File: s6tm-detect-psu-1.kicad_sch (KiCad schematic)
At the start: 60 parts, among them J1 USB_C_Receptacle_USB2.0_14P, J6 Conn_01x02, J7 Conn_01x02, U1 TPS62933, U3 TPS259470x, U5 TPS259470x, U7 TPS259470x, U8 TPS259470x

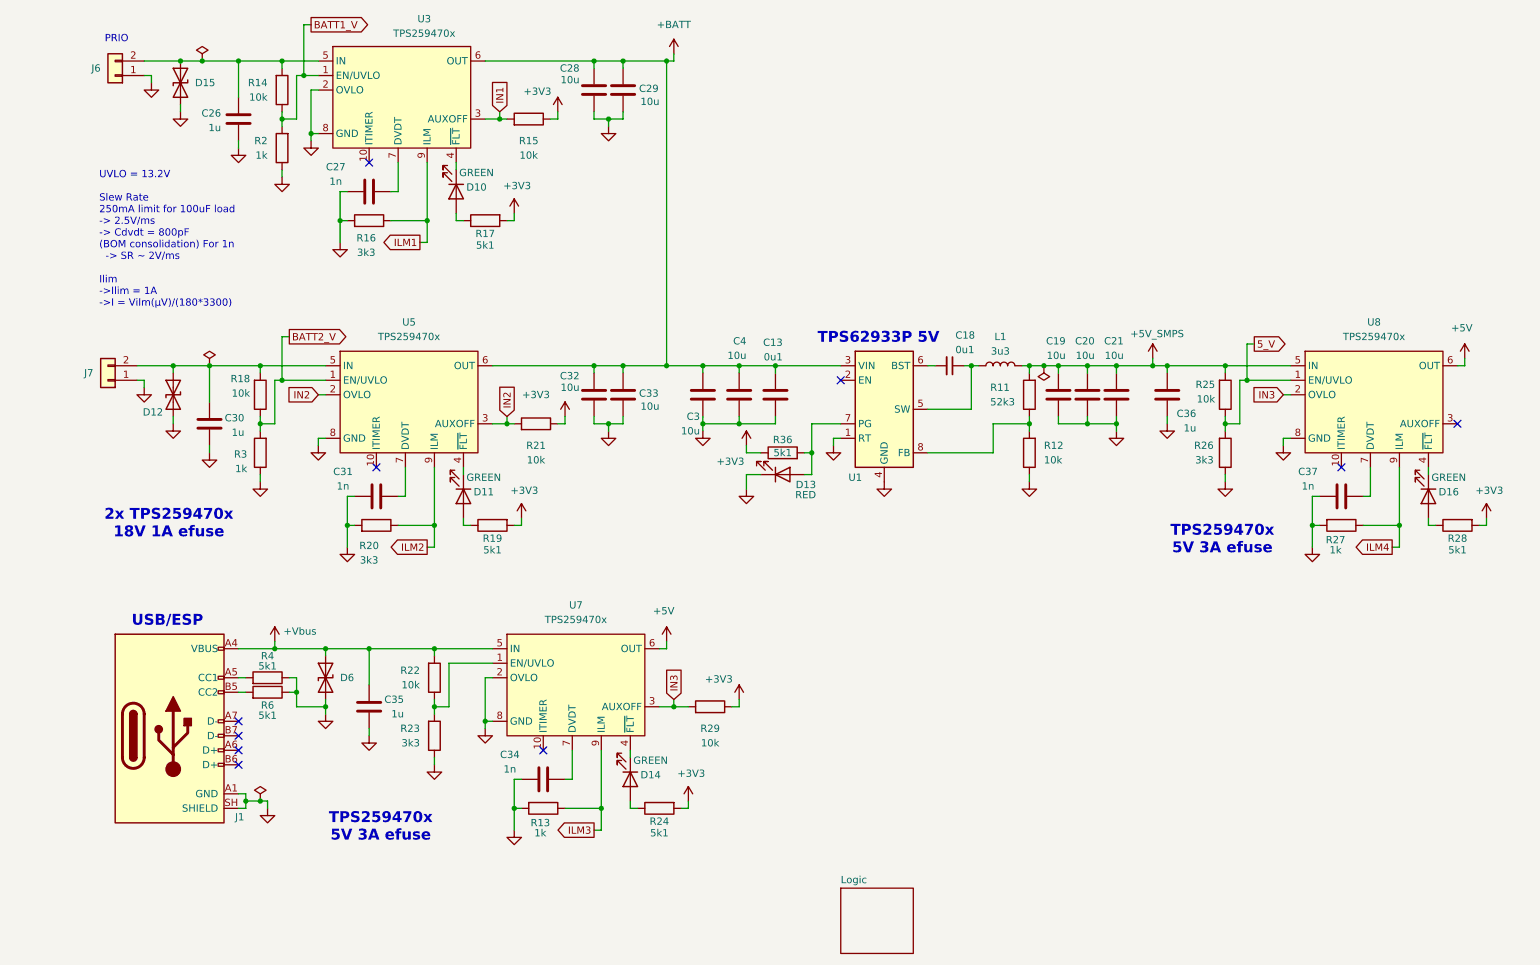
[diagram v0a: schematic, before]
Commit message: schem: add +5v bulk output caps
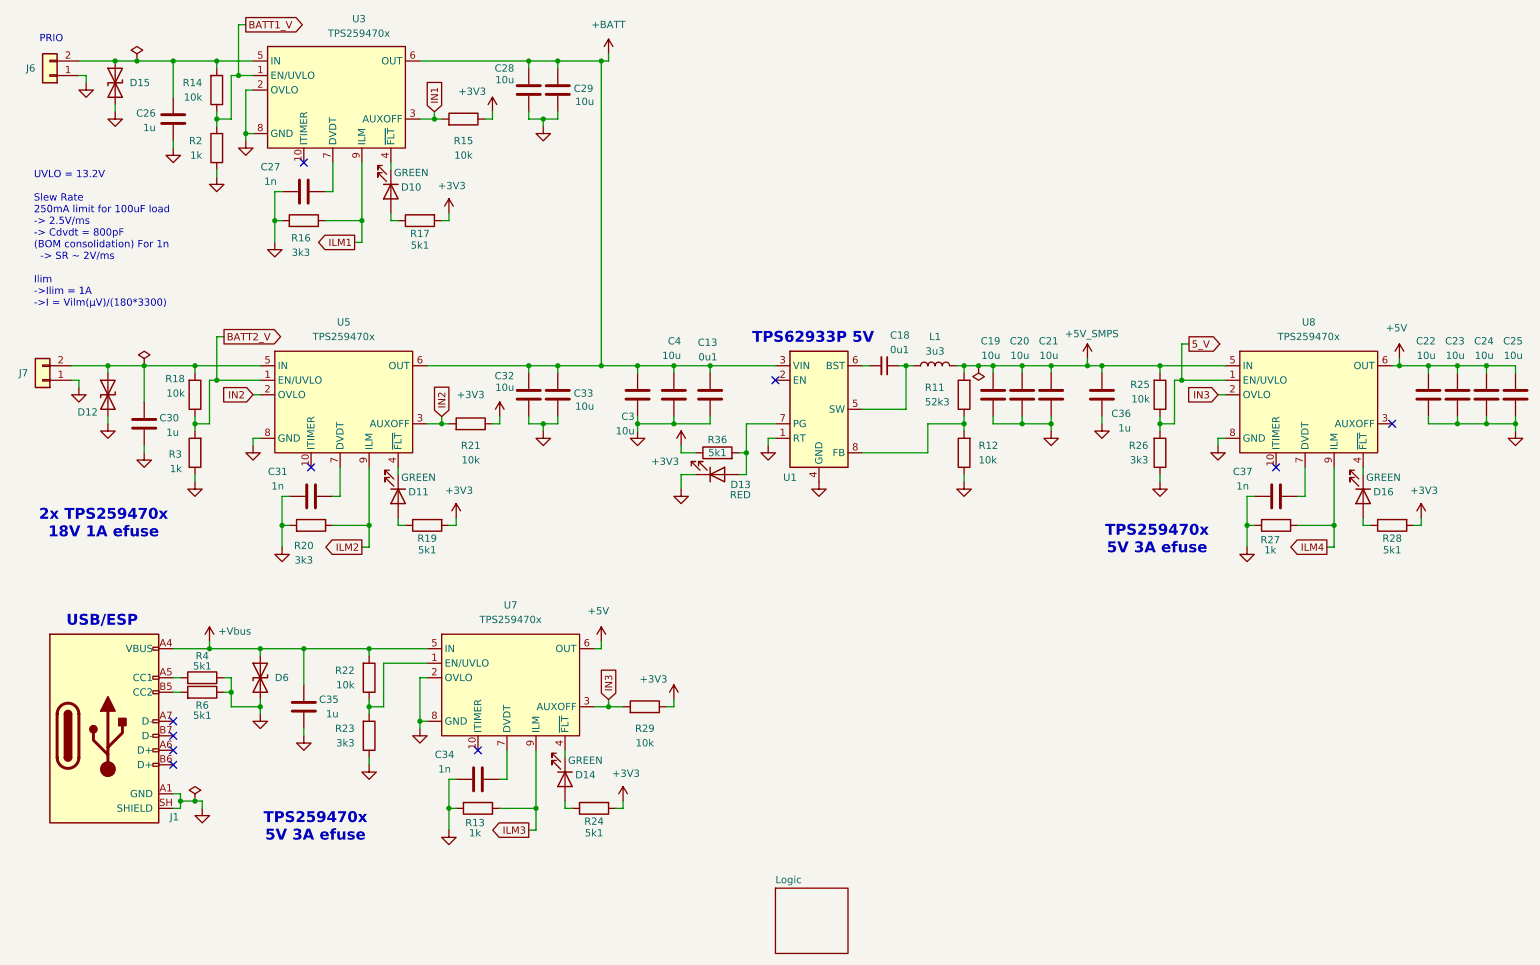
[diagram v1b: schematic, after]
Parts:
- added C22, C23, C24, C25: 10u, Capacitor_SMD:C_0805_2012Metric, symbol Device:C
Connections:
- net +5V: now also C22.1, C23.1, C24.1, C25.1
- net GND: now also C22.2, C23.2, C24.2, C25.2
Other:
- moved on the sheet: C13, C18, C19, C20, C21, C26, C27, C28, C29, C3, C30, C31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

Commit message: schem: connect efuses to mcu
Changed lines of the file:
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@@
 	)
 	(global_label "IN1"
-		(shape input)
+		(shape output)
 		(at 88.9 44.45 90)
 		(fields_autoplaced yes)
@@
 	)
 	(global_label "IN2"
-		(shape input)
+		(shape output)
 		(at 90.17 97.79 90)
 		(fields_autoplaced yes)
@@
 	)
 	(global_label "IN3"
-		(shape input)
+		(shape output)
 		(at 119.38 147.32 90)
 		(fields_autoplaced yes)

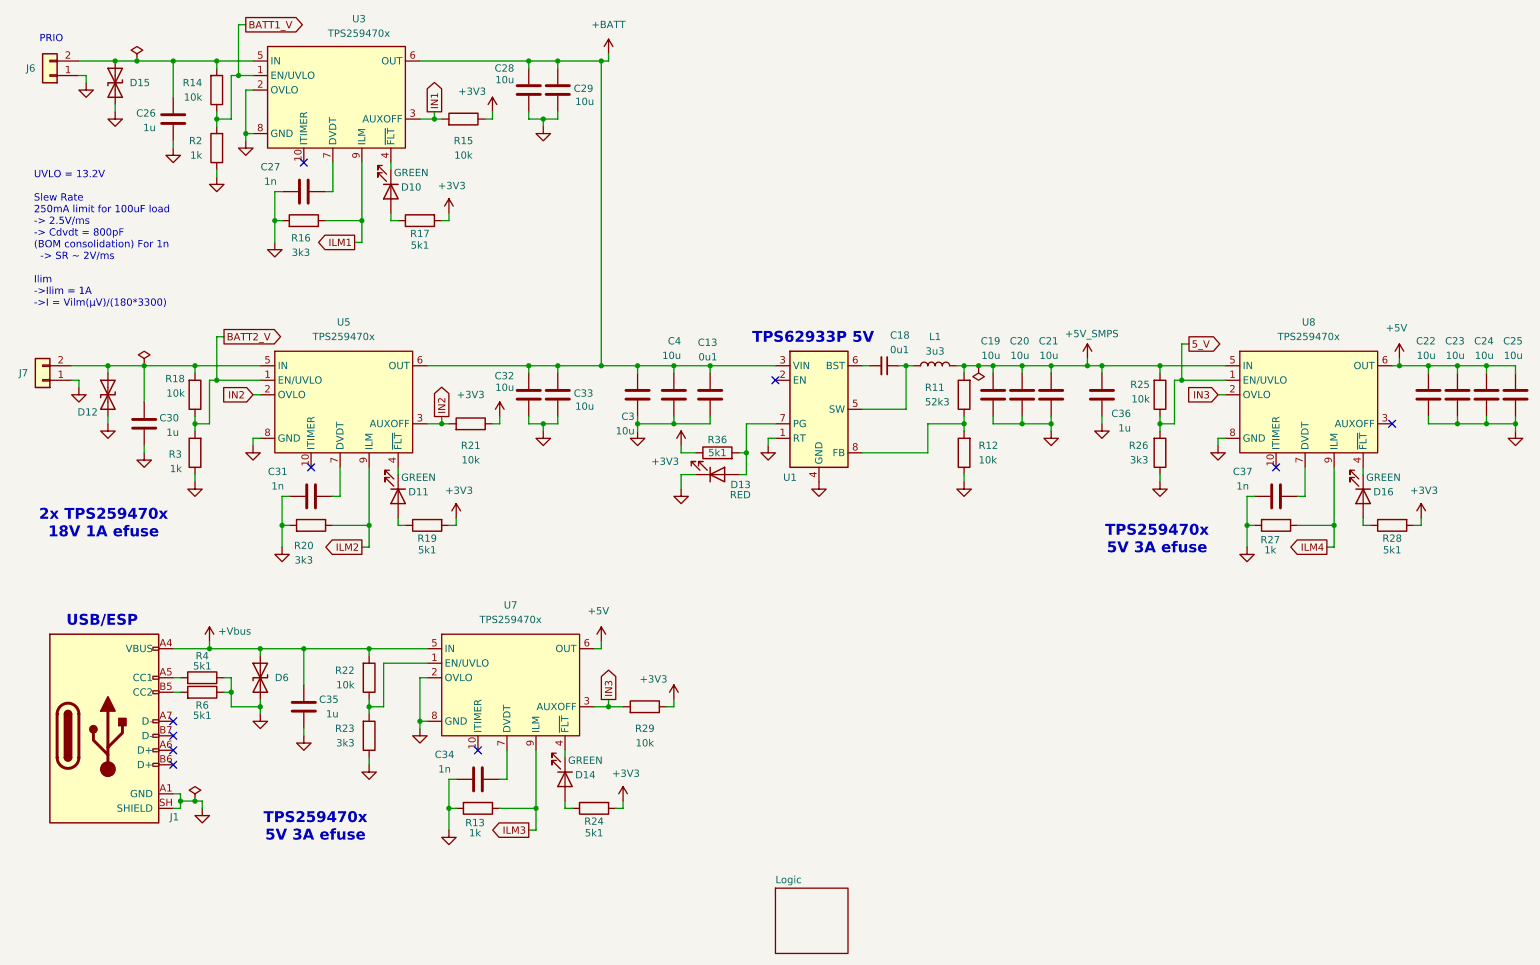
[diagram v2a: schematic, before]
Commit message: schem: add test points
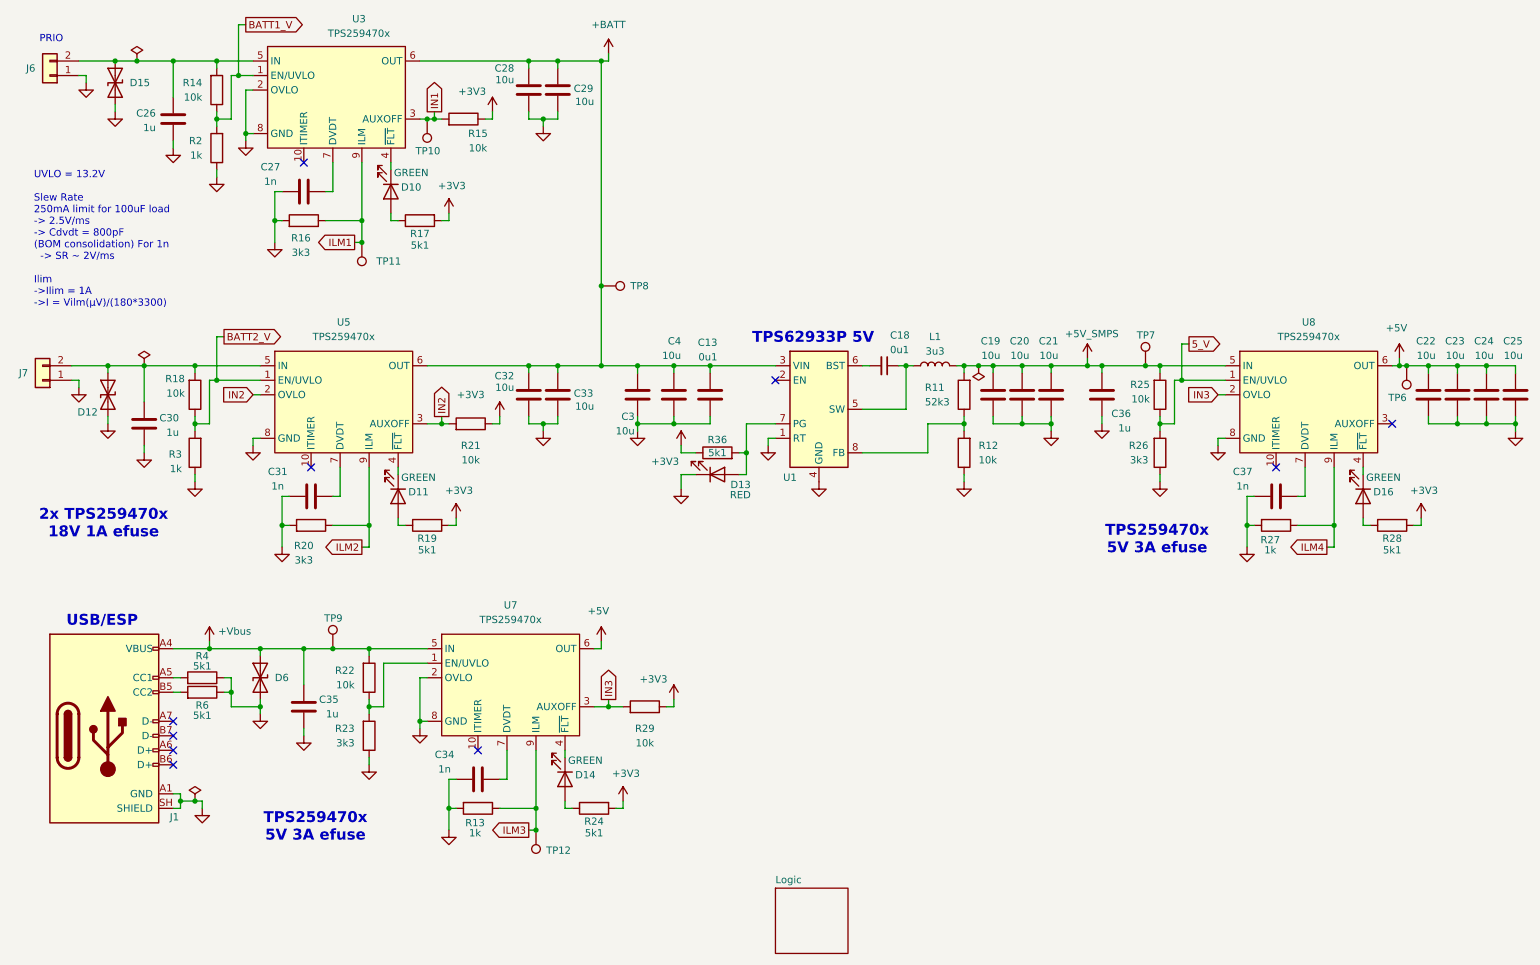
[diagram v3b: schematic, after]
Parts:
- added TP10, TP11, TP12, TP6, TP7, TP8, TP9: TestPoint, TestPoint:TestPoint_Pad_D2.0mm, symbol Connector:TestPoint
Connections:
- net +5V: now also TP6.1
- net +5V_SMPS: now also TP7.1
- net +BATT: now also TP8.1
- net +Vbus: now also TP9.1
- net ILM1: now also TP11.1
- net ILM3: now also TP12.1
- net IN1: now also TP10.1

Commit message: schem: add current measure jumpers
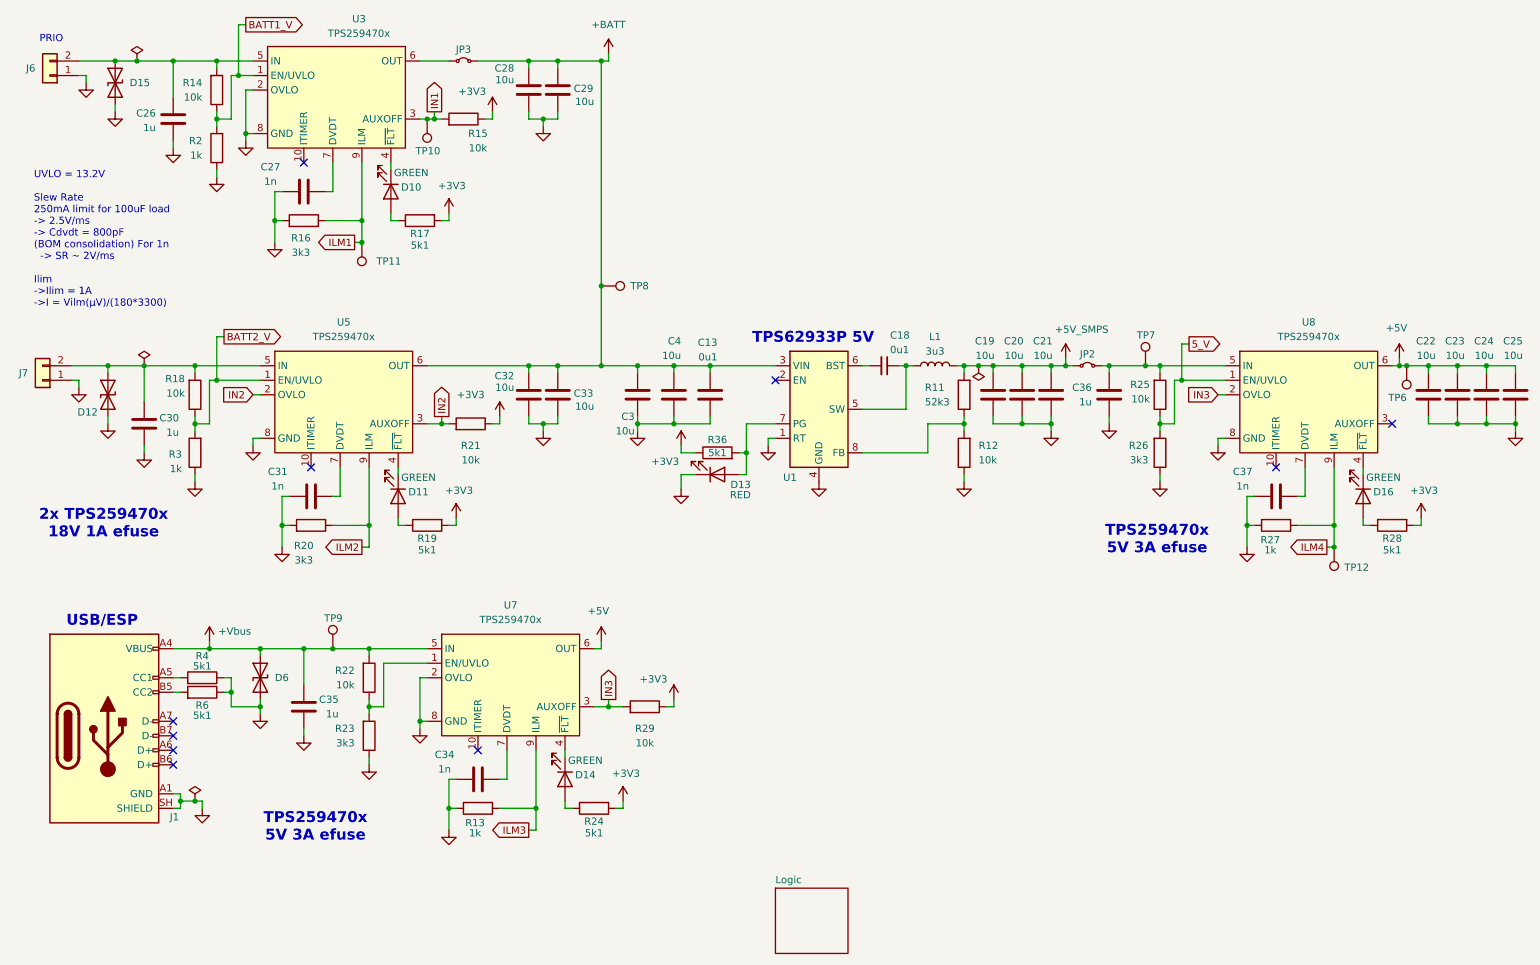
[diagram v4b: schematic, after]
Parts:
- added JP2, JP3: Jumper_2_Small_Bridged, Connector_PinHeader_2.54mm:PinHeader_1x02_P2.54mm_Vertical, symbol Jumper:Jumper_2_Small_Bridged
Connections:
- net +5V_SMPS: now also JP2.1 (A); no longer C36.2, R25.2, TP7.1, U8.5 (IN)
- net +BATT: now also JP3.2 (B); no longer U3.6 (OUT)
- net ILM3: no longer TP12.1
- net ILM4: now also TP12.1
- new net: C36.2, JP2.2 (B), R25.2, TP7.1, U8.5 (IN)
- new net: JP3.1 (A), U3.6 (OUT)
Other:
- moved on the sheet: C36

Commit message: schem: add missing parts to BOM
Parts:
- JP2, JP3: now left out of the parts list
- U3, U5, U7, U8: Basic (none) -> X; JLCPCB Part # (none) -> C3662799; Manufacturer (none) -> Texas Instruments; Manufacturer Part Number (none) -> TPS259470ARPWR
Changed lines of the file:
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@@
 			)
 		)
+		(property "Basic" "X"
+			(at 102.87 143.51 0)
+			(hide yes)
+			(show_name no)
+			(do_not_autoplace no)
+			(effects
+				(font
+					(size 1.27 1.27)
+				)
+			)
+		)
+		(property "JLCPCB Part #" "C3662799"
+			(at 102.87 143.51 0)
+			(hide yes)
+			(show_name no)
+			(do_not_autoplace no)
+			(effects
+				(font
+					(size 1.27 1.27)
+				)
+			)
+		)
+		(property "Manufacturer" "Texas Instruments"
+			(at 102.87 143.51 0)
+			(hide yes)
+			(show_name no)
+			(do_not_autoplace no)
+			(effects
+				(font
+					(size 1.27 1.27)
+				)
+			)
+		)
+		(property "Manufacturer Part Number" "TPS259470ARPWR"
+			(at 102.87 143.51 0)
+			(hide yes)
+			(show_name no)
+			(do_not_autoplace no)
+			(effects
+				(font
+					(size 1.27 1.27)
+				)
+			)
+		)
 		(pin "1"
 		)
@@
 			)
 		)
+		(property "Basic" "X"
+			(at 73.66 93.98 0)
+			(hide yes)
+			(show_name no)
+			(do_not_autoplace no)
+			(effects
+				(font
+					(size 1.27 1.27)
+				)
+			)
+		)
+		(property "JLCPCB Part #" "C3662799"
+			(at 73.66 93.98 0)
+			(hide yes)
+			(show_name no)
+			(do_not_autoplace no)
+			(effects
+				(font
+					(size 1.27 1.27)
+				)
+			)
+		)
+		(property "Manufacturer" "Texas Instruments"
+			(at 73.66 93.98 0)
+			(hide yes)
+			(show_name no)
+			(do_not_autoplace no)
+			(effects
+				(font
+					(size 1.27 1.27)
+				)
+			)
+		)
+		(property "Manufacturer Part Number" "TPS259470ARPWR"
+			(at 73.66 93.98 0)
+			(hide yes)
+			(show_name no)
+			(do_not_autoplace no)
+			(effects
+				(font
+					(size 1.27 1.27)
+				)
+			)
+		)
 		(pin "1"
 		)
@@
 		(body_style 1)
 		(exclude_from_sim no)
-		(in_bom yes)
+		(in_bom no)
 		(on_board yes)
 		(in_pos_files yes)
@@
 		(body_style 1)
 		(exclude_from_sim no)
-		(in_bom yes)
+		(in_bom no)
 		(on_board yes)
 		(in_pos_files yes)
@@
 			)
 		)
+		(property "Basic" "X"
+			(at 72.39 40.64 0)
+			(hide yes)
+			(show_name no)
+			(do_not_autoplace no)
+			(effects
+				(font
+					(size 1.27 1.27)
+				)
+			)
+		)
+		(property "JLCPCB Part #" "C3662799"
+			(at 72.39 40.64 0)
+			(hide yes)
+			(show_name no)
+			(do_not_autoplace no)
+			(effects
+				(font
+					(size 1.27 1.27)
+				)
+			)
+		)
+		(property "Manufacturer" "Texas Instruments"
+			(at 72.39 40.64 0)
+			(hide yes)
+			(show_name no)
+			(do_not_autoplace no)
+			(effects
+				(font
+					(size 1.27 1.27)
+				)
+			)
+		)
+		(property "Manufacturer Part Number" "TPS259470ARPWR"
+			(at 72.39 40.64 0)
+			(hide yes)
+			(show_name no)
+			(do_not_autoplace no)
+			(effects
+				(font
+					(size 1.27 1.27)
+				)
+			)
+		)
 		(pin "1"
 		)
@@
 			(at 242.57 93.98 0)
 			(hide yes)
+			(show_name no)
+			(do_not_autoplace no)
+			(effects
+				(font
+					(size 1.27 1.27)
+				)
+			)
+		)
+		(property "Basic" "X"
+			(at 242.57 93.98 0)
+			(hide yes)
+			(show_name no)
+			(do_not_autoplace no)
+			(effects
+				(font
+					(size 1.27 1.27)
+				)
+			)
+		)
+		(property "JLCPCB Part #" "C3662799"
+			(at 242.57 93.98 0)
+			(hide yes)
+			(show_name no)
+			(do_not_autoplace no)
+			(effects
+				(font
+					(size 1.27 1.27)
+				)
+			)
+		)
+		(property "Manufacturer" "Texas Instruments"
+			(at 242.57 93.98 0)
+			(hide yes)
+			(show_name no)
+			(do_not_autoplace no)
+			(effects
+				(font
+					(size 1.27 1.27)
+				)
+			)
+		)
+		(property "Manufacturer Part Number" "TPS259470ARPWR"
+			(at 242.57 93.98 0)
+			(hide yes)

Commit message: schem: add title
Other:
- company: (none) -> Rémi Ait-Younes
- title: (none) -> S6TM Detect PSU 1
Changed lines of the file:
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@@
 	(generator_version "10.0")
 	(paper "A4")
+	(title_block
+		(title "S6TM Detect PSU 1")
+		(date "2026-09-16")
+		(rev "01")
+		(company "Rémi Ait-Younes")
+	)
 	(text "TPS259470x\n5V 3A efuse"
 		(exclude_from_sim no)

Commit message: schem: renummber
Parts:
- renumbered C30 to C1, C33 to C10, C3 to C11, C4 to C12, C18 to C14, C19 to C15, C20 to C16, C21 to C17, C36 to C18, C37 to C19, C26 to C2, C22 to C20, C23 to C21, C24 to C22, C25 to C23, C27 to C3, C35 to C4, C31 to C5, C34 to C6, C28 to C7, C32 to C8, C29 to C9, D12 to D1, D15 to D2, D6 to D3, D10 to D4, D11 to D5, D14 to D6, D13 to D7, D16 to D8, J7 to J1, J6 to J2, J1 to J3, JP3 to JP1, R18 to R1, R23 to R10, R17 to R11, R19 to R12, R15 to R13, R21 to R14, R13 to R15, R24 to R16, R29 to R17, R36 to R18, R11 to R19, R3 to R2, R12 to R20, R25 to R21, R26 to R22, R27 to R23, R28 to R24, R4 to R3, R6 to R4, R14 to R5, R2 to R6, R16 to R7, R20 to R8, R22 to R9, TP9 to TP1, TP11 to TP2, TP10 to TP3, TP8 to TP4, TP7 to TP5, TP12 to TP6, TP6 to TP7, U3 to U1, U5 to U2, U7 to U3, U1 to U4, U8 to U5

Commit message: schem: update 2x 2ipn xh header footprint
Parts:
- J1, J2: footprint Connector_JST:JST_XH_B2B-XH-A_1x02_P2.50mm_Vertical -> Connector_JST:JST_XH_S2B-XH-A-1_1x02_P2.50mm_Horizontal; JLCPCB Part # C495685 -> C163035; Manufacturer Part Number B2B-XH-A-R(LF)(SN) -> S2B-XH-A-1(LF)(SN)
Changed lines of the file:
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@@
 			)
 		)
-		(property "Footprint" "Connector_JST:JST_XH_B2B-XH-A_1x02_P2.50mm_Vertical"
+		(property "Footprint" "Connector_JST:JST_XH_S2B-XH-A-1_1x02_P2.50mm_Horizontal"
 			(at 20.32 91.44 0)
 			(hide yes)
@@
 			)
 		)
-		(property "JLCPCB Part #" "C495685"
+		(property "JLCPCB Part #" "C163035"
 			(at 20.32 91.44 0)
 			(hide yes)
@@
 			)
 		)
-		(property "Manufacturer Part Number" "B2B-XH-A-R(LF)(SN)"
+		(property "Manufacturer Part Number" "S2B-XH-A-1(LF)(SN)"
 			(at 20.32 91.44 0)
 			(hide yes)
@@
 			)
 		)
-		(property "Footprint" "Connector_JST:JST_XH_B2B-XH-A_1x02_P2.50mm_Vertical"
+		(property "Footprint" "Connector_JST:JST_XH_S2B-XH-A-1_1x02_P2.50mm_Horizontal"
 			(at 21.59 38.1 0)
 			(hide yes)
@@
 			)
 		)
-		(property "JLCPCB Part #" "C495685"
+		(property "JLCPCB Part #" "C163035"
 			(at 21.59 38.1 0)
 			(hide yes)
@@
 			)
 		)
-		(property "Manufacturer Part Number" "B2B-XH-A-R(LF)(SN)"
+		(property "Manufacturer Part Number" "S2B-XH-A-1(LF)(SN)"
 			(at 21.59 38.1 0)
 			(hide yes)
